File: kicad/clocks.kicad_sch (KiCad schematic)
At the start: 38 parts, among them U1 SIT5156A, U2 ICE40LP384-SG32, U3 LMK1C1104, U4 LEA-M8T, U5 TDC7200, U6 LMK1C1104

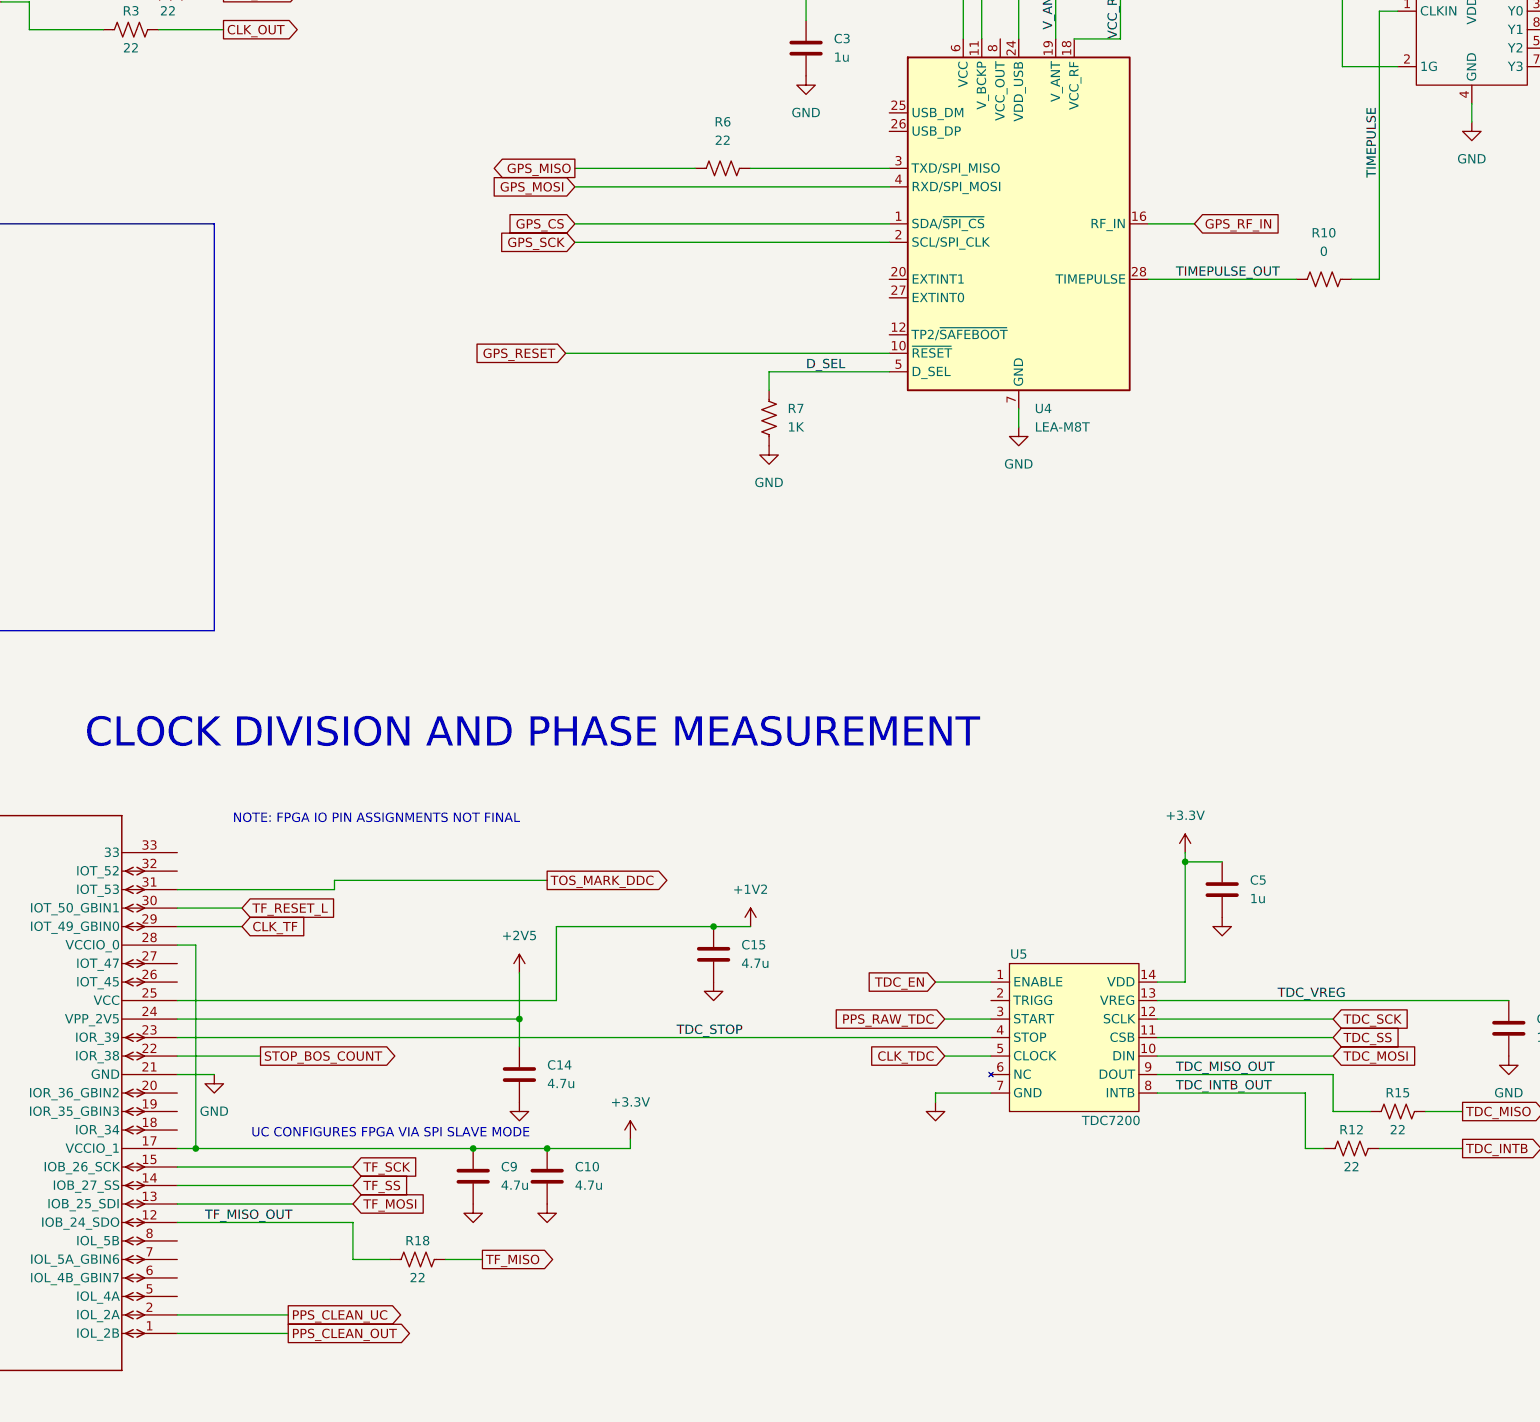
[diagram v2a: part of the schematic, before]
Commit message: wire up mcu
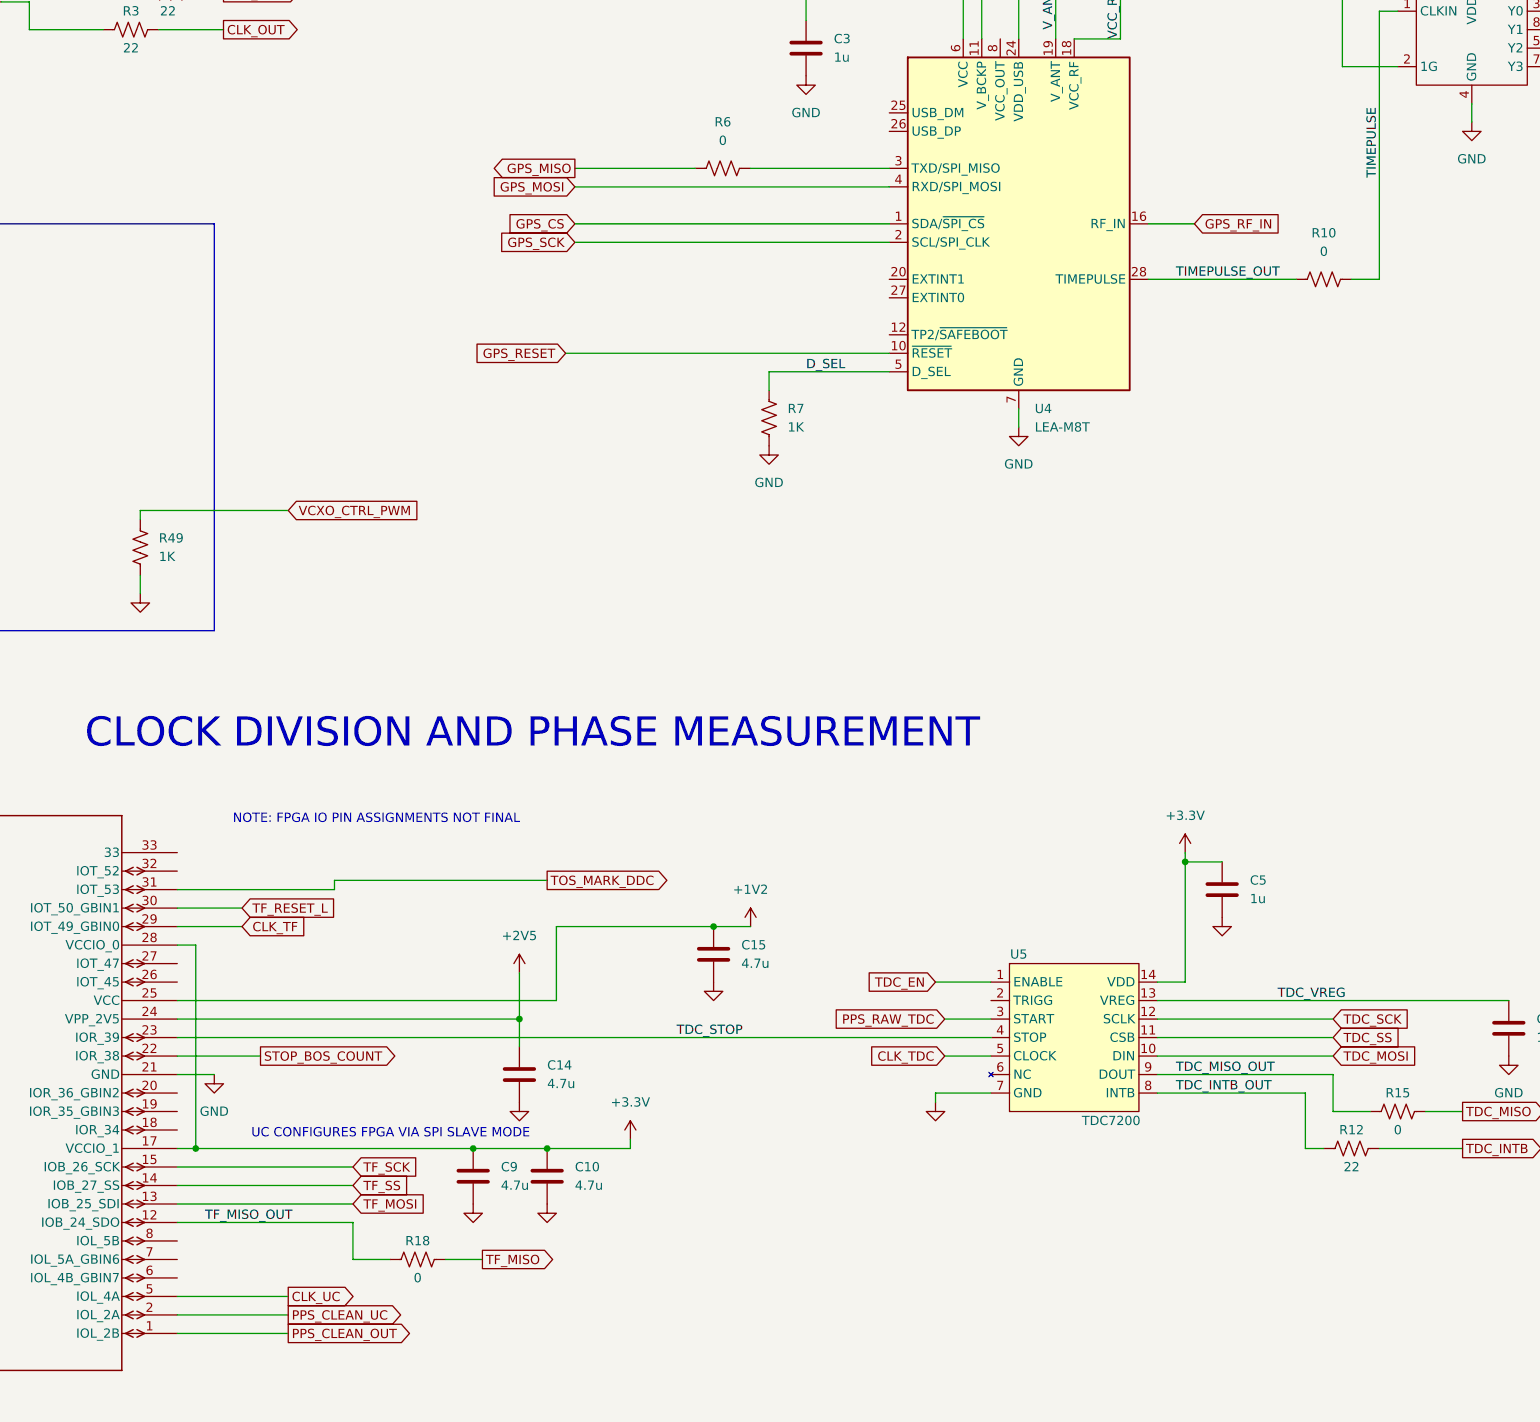
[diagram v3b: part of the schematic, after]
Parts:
- added R49: 1K, symbol Device:R_US
- R15, R18, R6: value 22 -> 0
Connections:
- net GND: now also R49.2
- net CLK_UC: now reaches U2.5 (IOL_4A)
- new net VCXO_CTRL_PWM: R49.1
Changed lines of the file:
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@@
+    (stroke (width 0) (type default))
+  )
+  (wire (pts (xy 165.1 132.08) (xy 165.1 133.35))
     (stroke (width 0) (type default))
   )
@@
     (stroke (width 0) (type default))
   )
+  (wire (pts (xy 185.42 132.08) (xy 165.1 132.08))
+    (stroke (width 0) (type default))
+  )
   (wire (pts (xy 372.11 64.77) (xy 367.03 64.77))
     (stroke (width 0) (type default))
@@
     (stroke (width 0) (type default))
   )
+  (wire (pts (xy 170.18 240.03) (xy 185.42 240.03))
+    (stroke (width 0) (type default))
+  )
   (wire (pts (xy 160.02 66.04) (xy 149.86 66.04))
     (stroke (width 0) (type default))
@@
   )
   (wire (pts (xy 367.03 64.77) (xy 367.03 66.04))
+    (stroke (width 0) (type default))
+  )
+  (wire (pts (xy 165.1 140.97) (xy 165.1 143.51))
     (stroke (width 0) (type default))
   )
@@
     )
   )
+  (global_label "VCXO_CTRL_PWM" (shape input) (at 185.42 132.08 0) (fields_autoplaced)
+    (effects (font (size 1.27 1.27)) (justify left))
+    (property "Intersheetrefs" "${INTERSHEET_REFS}" (at 203.9475 132.08 0)
+      (effects (font (size 1.27 1.27)) (justify left) hide)
+    )
+  )
   (global_label "CLK_TF" (shape input) (at 179.07 189.23 0) (fields_autoplaced)
     (effects (font (size 1.27 1.27)) (justify left))
@@
     (effects (font (size 1.27 1.27)) (justify left))
     (property "Intersheetrefs" "${INTERSHEET_REFS}" (at 186.1071 55.88 0)
+      (effects (font (size 1.27 1.27)) (justify left) hide)
+    )
+  )
+  (global_label "CLK_UC" (shape output) (at 185.42 240.03 0) (fields_autoplaced)
+    (effects (font (size 1.27 1.27)) (justify left))
+    (property "Intersheetrefs" "${INTERSHEET_REFS}" (at 195.5414 240.03 0)
       (effects (font (size 1.27 1.27)) (justify left) hide)
     )
@@
     )
   )
+  (symbol (lib_id "Device:R_US") (at 165.1 137.16 0) (unit 1)
+    (in_bom yes) (on_board yes) (dnp no) (fields_autoplaced)
+    (property "Reference" "R49" (at 167.64 135.89 0)
+      (effects (font (size 1.27 1.27)) (justify left))
+    )
+    (property "Value" "1K" (at 167.64 138.43 0)
+      (effects (font (size 1.27 1.27)) (justify left))
+    )
+    (property "Footprint" "" (at 166.116 137.414 90)
+      (effects (font (size 1.27 1.27)) hide)
+    )
+    (property "Datasheet" "~" (at 165.1 137.16 0)
+      (effects (font (size 1.27 1.27)) hide)
+    )
+    (pin "1")
+    (pin "2")
+    (instances
+      (project "gpsrx"
+        (path "/c3c549bc-9d82-4b6a-bdb9-a3870905229d/70e7e3a4-572d-4c59-9c26-94e3cd20e23c"
+          (reference "R49") (unit 1)
+        )
+      )
+    )
+  )
   (symbol (lib_id "power:PWR_FLAG") (at 265.43 38.1 0) (unit 1)
     (in_bom yes) (on_board yes) (dnp no) (fields_autoplaced)
@@
       (effects (font (size 1.27 1.27)))
     )
-    (property "Value" "22" (at 203.2 237.49 90)
+    (property "Value" "0" (at 203.2 237.49 90)
       (effects (font (size 1.27 1.27)))
     )
@@
       (effects (font (size 1.27 1.27)))
     )
-    (property "Value" "22" (at 337.82 217.17 90)
+    (property "Value" "0" (at 337.82 217.17 90)
       (effects (font (size 1.27 1.27)))
     )
@@
       (effects (font (size 1.27 1.27)))
     )
-    (property "Value" "22" (at 245.11 81.28 90)
+    (property "Value" "0" (at 245.11 81.28 90)
       (effects (font (size 1.27 1.27)))
     )
@@
         )
       )
+    )
+  )
+  (symbol (lib_id "power:GND") (at 165.1 143.51 0) (unit 1)
+    (in_bom yes) (on_board yes) (dnp no) (fields_autoplaced)
+    (property "Reference" "#PWR093" (at 165.1 149.86 0)
+      (effects (font (size 1.27 1.27)) hide)
+    )
+    (property "Value" "GND" (at 165.1 148.59 0)
+      (effects (font (size 1.27 1.27)) hide)
+    )
+    (property "Footprint" "" (at 165.1 143.51 0)
+      (effects (font (size 1.27 1.27)) hide)
+    )
+    (property "Datasheet" "" (at 165.1 143.51 0)
+      (effects (font (size 1.27 1.27)) hide)
+    )
+    (pin "1")
+    (instances
+      (project "gpsrx"
+        (path "/c3c549bc-9d82-4b6a-bdb9-a3870905229d/70e7e3a4-572d-4c59-9c26-94e3cd20e23c"
+          (reference "#PWR093") (unit 1)
+        )
+      )

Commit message: fix ercs
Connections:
- net PPS_RAW_LOGIC: now also U2.26 (IOT_45)
- net GPS_CS renamed GPS_SS
- net GPS_RESET renamed GPS_RESET_L
- net TF_CRST renamed TF_CRST_L
- no-connect marks 0 -> 16
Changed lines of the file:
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@@
   (junction (at 48.26 245.11) (diameter 0) (color 0 0 0 0)
   )
+  (no_connect (at 170.18 217.17))
+  (no_connect (at 170.18 179.07))
+  (no_connect (at 267.97 80.01))
+  (no_connect (at 267.97 77.47))
+  (no_connect (at 170.18 181.61))
+  (no_connect (at 170.18 212.09))
+  (no_connect (at 170.18 232.41))
+  (no_connect (at 283.21 67.31))
+  (no_connect (at 170.18 237.49))
+  (no_connect (at 170.18 194.31))
+  (no_connect (at 281.94 199.39))
+  (no_connect (at 170.18 214.63))
+  (no_connect (at 267.97 107.95))
+  (no_connect (at 267.97 102.87))
+  (no_connect (at 170.18 234.95))
+  (no_connect (at 267.97 100.33))
   (wire (pts (xy 69.85 33.02) (xy 69.85 46.99))
     (stroke (width 0) (type default))
@@
   )
   (wire (pts (xy 377.19 59.69) (xy 361.95 59.69))
+    (stroke (width 0) (type default))
+  )
+  (wire (pts (xy 170.18 196.85) (xy 179.07 196.85))
     (stroke (width 0) (type default))
   )
@@
     )
   )
-  (global_label "GPS_CS" (shape input) (at 224.79 92.71 180) (fields_autoplaced)
-    (effects (font (size 1.27 1.27)) (justify right))
-    (property "Intersheetrefs" "${INTERSHEET_REFS}" (at 214.6082 92.71 0)
+  (global_label "GPS_SS" (shape input) (at 224.79 92.71 180) (fields_autoplaced)
+    (effects (font (size 1.27 1.27)) (justify right))
+    (property "Intersheetrefs" "${INTERSHEET_REFS}" (at 214.6687 92.71 0)
       (effects (font (size 1.27 1.27)) (justify right) hide)
     )
@@
     )
   )
-  (global_label "TF_CRST" (shape input) (at 54.61 186.69 180) (fields_autoplaced)
-    (effects (font (size 1.27 1.27)) (justify right))
-    (property "Intersheetrefs" "${INTERSHEET_REFS}" (at 43.8839 186.69 0)
-      (effects (font (size 1.27 1.27)) (justify right) hide)
+  (global_label "TF_CRST_L" (shape input) (at 54.61 186.69 180) (fields_autoplaced)
+    (effects (font (size 1.27 1.27)) (justify right))
+    (property "Intersheetrefs" "${INTERSHEET_REFS}" (at 41.8882 186.69 0)
+      (effects (font (size 1.27 1.27)) (justify right) hide)
+    )
+  )
+  (global_label "PPS_RAW_LOGIC" (shape input) (at 179.07 196.85 0) (fields_autoplaced)
+    (effects (font (size 1.27 1.27)) (justify left))
+    (property "Intersheetrefs" "${INTERSHEET_REFS}" (at 197.0533 196.85 0)
+      (effects (font (size 1.27 1.27)) (justify left) hide)
     )
   )
@@
     )
   )
-  (global_label "GPS_RESET" (shape input) (at 223.52 110.49 180) (fields_autoplaced)
-    (effects (font (size 1.27 1.27)) (justify right))
-    (property "Intersheetrefs" "${INTERSHEET_REFS}" (at 210.0726 110.49 0)
-      (effects (font (size 1.27 1.27)) (justify right) hide)
-    )
+  (global_label "GPS_RESET_L" (shape input) (at 223.52 110.49 180) (fields_autoplaced)
+    (effects (font (size 1.27 1.27)) (justify right))
+    (property "Intersheetrefs" "${INTERSHEET_REFS}" (at 208.0769 110.49 0)
+      (effects (font (size 1.27 1.27)) (justify right) hide)
+    )
